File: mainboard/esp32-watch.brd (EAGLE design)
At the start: 63.5 x 38.1 mm, 15 parts, among them J1 CON-MOLEX_0532610671, U1 ESP-WROOM-32

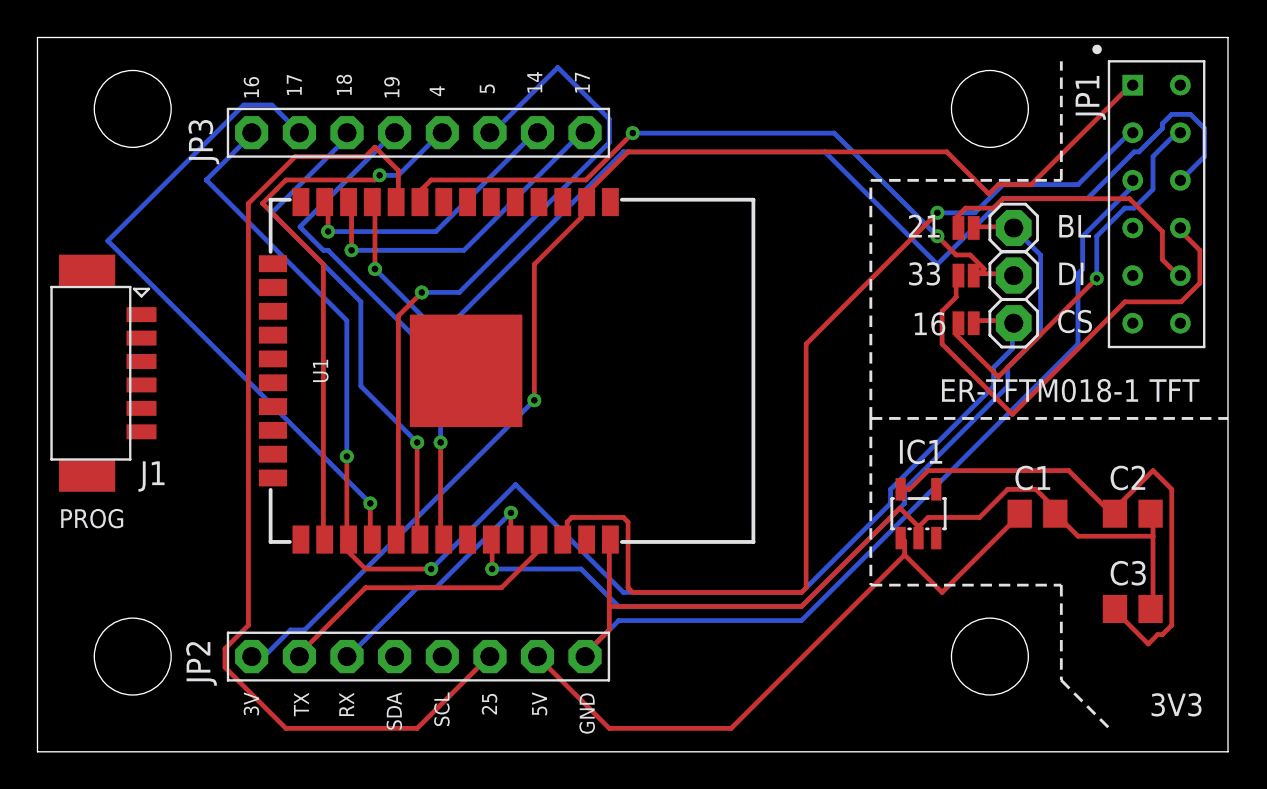
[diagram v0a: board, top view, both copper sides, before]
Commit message: started to add NRF24L01 header
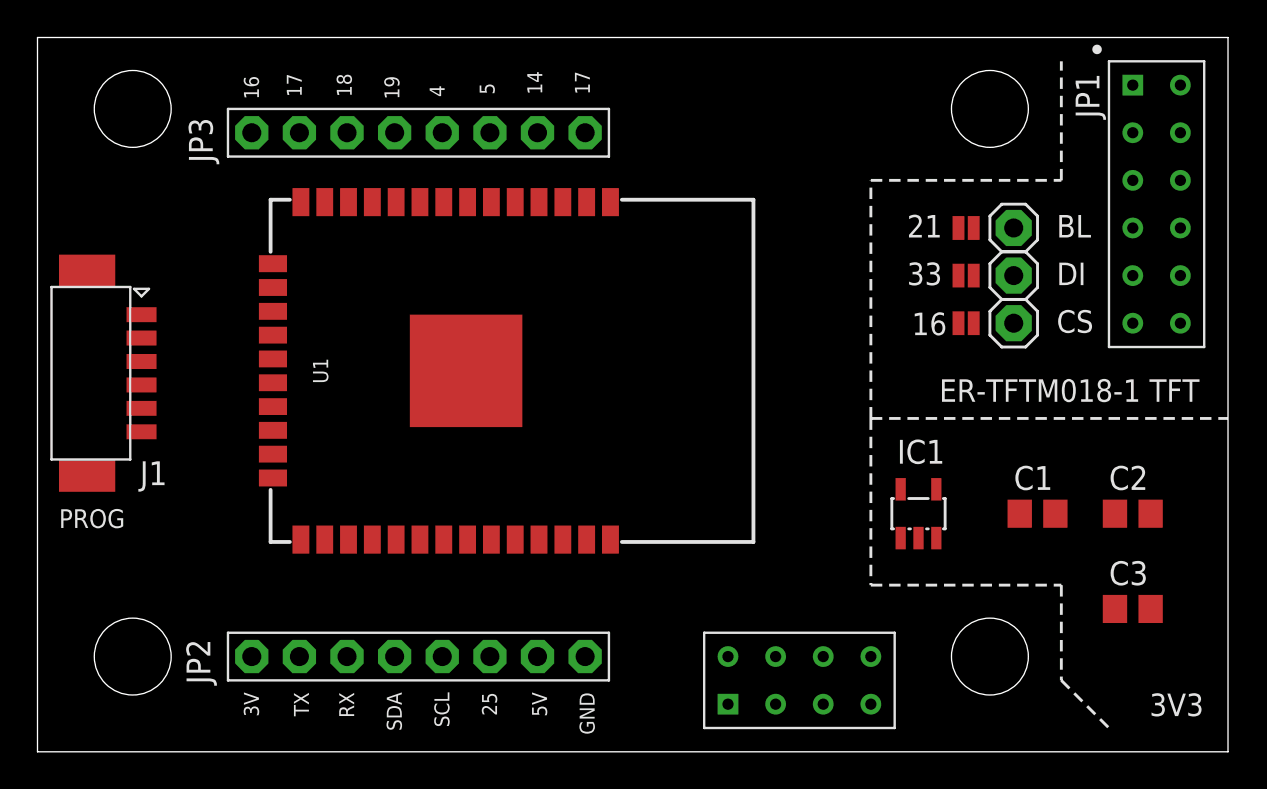
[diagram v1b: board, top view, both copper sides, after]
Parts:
- added U$1: NRF24L01, VanEagleLib:NRF24L01-MODULE
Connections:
- net 3V3: now also U$1.2
- net GND: now also U$1.1
- net IO18: now also U$1.7
- net IO19: now also U$1.5
- net IO21: now also U$1.6
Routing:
- net GND: track 89.6 -> 0.00 mm
- net IO16: track 77.0 -> 0.00 mm, vias 2 -> 0
- net 3V3: track 66.3 -> 0.00 mm, vias 1 -> 0
- net IO26: track 63.0 -> 0.00 mm, vias 1 -> 0
- net IO25: track 53.8 -> 0.00 mm
- net IO22: track 52.8 -> 0.00 mm, vias 1 -> 0
- net IO21: track 47.1 -> 0.00 mm, vias 1 -> 0
- net IO33: track 37.9 -> 0.00 mm, vias 2 -> 0
- net IO5: track 37.3 -> 0.00 mm, vias 1 -> 0
- net IO17: track 35.6 -> 0.00 mm, vias 1 -> 0
- net +5V: track 34.7 -> 0.00 mm
- net IO4: track 30.4 -> 0.00 mm, vias 1 -> 0
- net +3V3: track 29.1 -> 0.00 mm
- net IO19: track 27.1 -> 0.00 mm, vias 1 -> 0
- net IO18: track 26.9 -> 0.00 mm, vias 1 -> 0
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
